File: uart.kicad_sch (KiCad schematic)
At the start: 0 parts

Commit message: Finally done the layout
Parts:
- added J6: Conn_01x03_Pin, Connector_PinHeader_2.54mm:PinHeader_1x03_P2.54mm_Vertical, symbol Connector:Conn_01x03_Pin
- added TP1, TP2, TP3, TP4: TestPoint, TestPoint:TestPoint_Pad_D1.0mm, symbol Connector:TestPoint
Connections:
- new net GND: J6.1 (Pin_1)
- new net MAVLINK_RX: J6.3 (Pin_3)
- new net MAVLINK_TX: J6.2 (Pin_2)
- new net UART3_RX: TP1.1
- new net UART3_TX: TP2.1
- new net UART7_RX: TP3.1
- new net UART7_TX: TP4.1

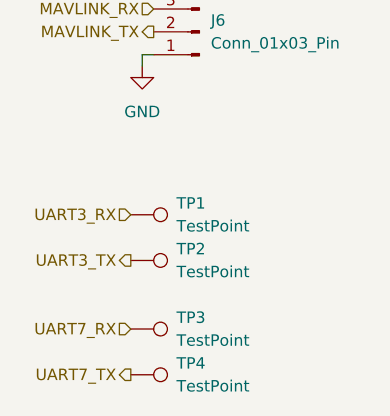
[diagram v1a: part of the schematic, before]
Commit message: Finalized layout, added more detailed 3d models
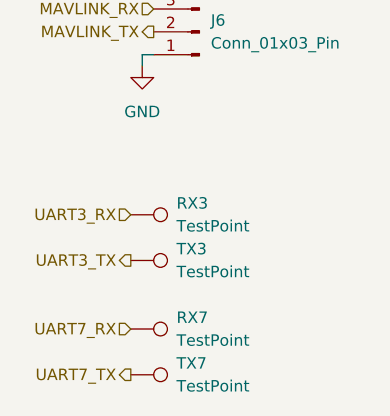
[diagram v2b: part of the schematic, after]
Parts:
- renumbered TP1 to RX3, TP3 to RX7, TP2 to TX3, TP4 to TX7
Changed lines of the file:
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@@
 		(dnp no)
 		(fields_autoplaced yes)
-		(property "Reference" "TP3"
+		(property "Reference" "RX7"
 			(at 119.38 87.6299 90)
 			(effects
@@
 			(project "LTELink"
 				(path "/ebd96e19-6f65-4022-a6da-be26c0716f8e/1f51a8cf-4ed0-4d00-bcb9-e34ac73c8e7e"
-					(reference "TP3")
+					(reference "RX7")
 					(unit 1)
 				)
@@
 		(dnp no)
 		(fields_autoplaced yes)
-		(property "Reference" "TP1"
+		(property "Reference" "RX3"
 			(at 119.38 74.9299 90)
 			(effects
@@
 			(project ""
 				(path "/ebd96e19-6f65-4022-a6da-be26c0716f8e/1f51a8cf-4ed0-4d00-bcb9-e34ac73c8e7e"
-					(reference "TP1")
+					(reference "RX3")
 					(unit 1)
 				)
@@
 		(dnp no)
 		(fields_autoplaced yes)
-		(property "Reference" "TP2"
+		(property "Reference" "TX3"
 			(at 119.38 80.0099 90)
 			(effects
@@
 			(project "LTELink"
 				(path "/ebd96e19-6f65-4022-a6da-be26c0716f8e/1f51a8cf-4ed0-4d00-bcb9-e34ac73c8e7e"
-					(reference "TP2")
+					(reference "TX3")
 					(unit 1)
 				)
@@
 		(dnp no)
 		(fields_autoplaced yes)
-		(property "Reference" "TP4"
+		(property "Reference" "TX7"
 			(at 119.38 92.7099 90)
 			(effects
@@
 			(project "LTELink"
 				(path "/ebd96e19-6f65-4022-a6da-be26c0716f8e/1f51a8cf-4ed0-4d00-bcb9-e34ac73c8e7e"
-					(reference "TP4")
-					(unit 1)
-				)
+					(reference "TX7")
+					(unit 1)
+				)

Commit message: finalized board for fabrication
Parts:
- J6, RX3, RX7, TX3, TX7: now not fitted

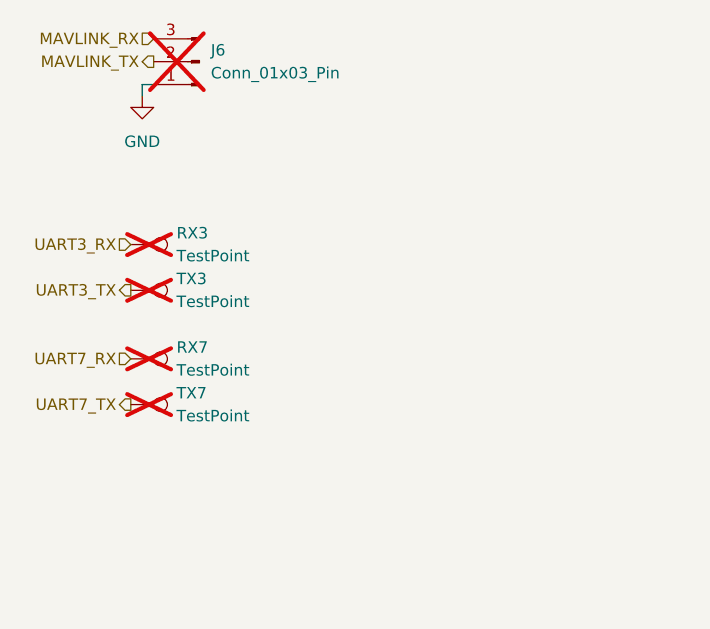
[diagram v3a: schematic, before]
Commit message: fix incorrect footprint orientation and breakout uarts
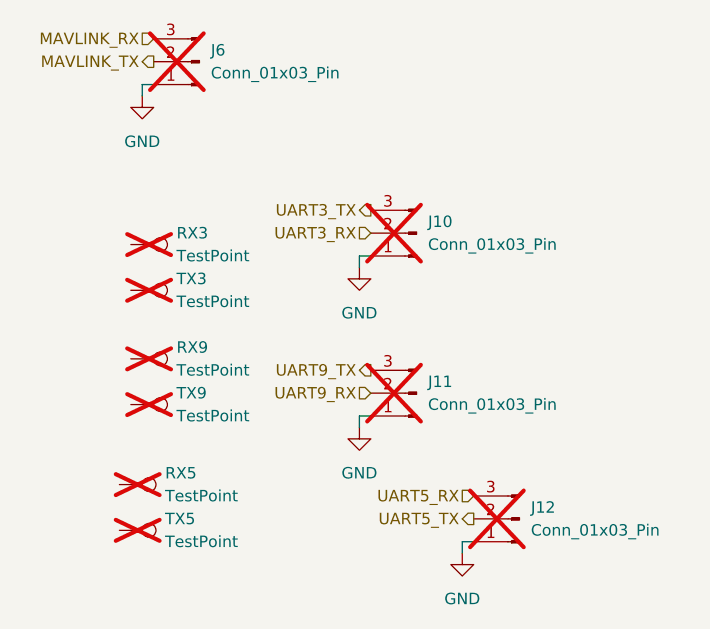
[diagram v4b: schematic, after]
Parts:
- added J10, J11, J12: Conn_01x03_Pin, Connector_PinHeader_2.54mm:PinHeader_1x03_P2.54mm_Vertical, symbol Connector:Conn_01x03_Pin
- added RX5, TX5: TestPoint, TestPoint:TestPoint_Pad_D1.0mm, symbol Connector:TestPoint
- renumbered RX7 to RX9, TX7 to TX9
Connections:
- net GND: now also J10.1 (Pin_1), J11.1 (Pin_1), J12.1 (Pin_1)
- net UART3_RX: now also J10.2 (Pin_2); no longer RX3.1
- net UART3_TX: now also J10.3 (Pin_3); no longer TX3.1
- net UART7_RX: no longer names the net of RX9.1
- net UART7_TX: no longer names the net of TX9.1
- new net UART5_RX: J12.3 (Pin_3)
- new net UART5_TX: J12.2 (Pin_2)
- new net UART9_RX: J11.2 (Pin_2)
- new net UART9_TX: J11.3 (Pin_3)
